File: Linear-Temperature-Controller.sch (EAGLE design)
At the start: 51 parts, among them IC1 LM393D, IC2 MEGA8-AI, IC3 AD5624R, IC4 AD5262, T1 MMBT3904, T2 MMBT3904

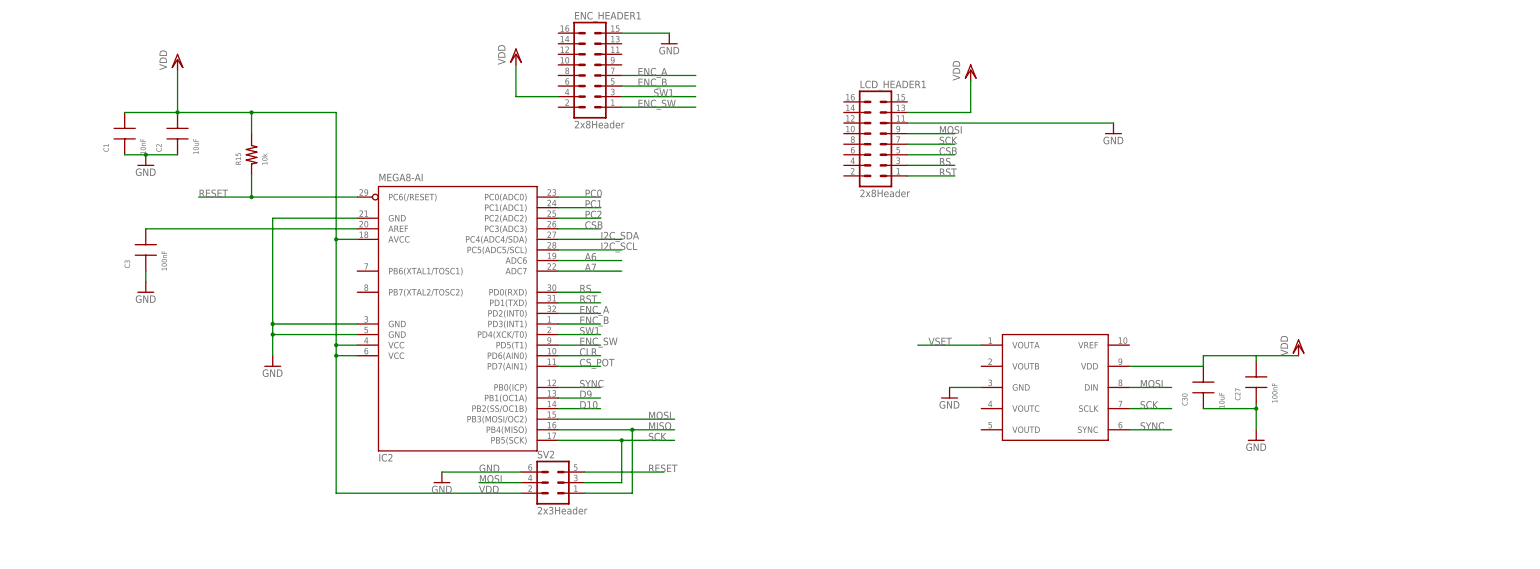
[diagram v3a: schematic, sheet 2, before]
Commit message: Replace microcontroller with Teensy
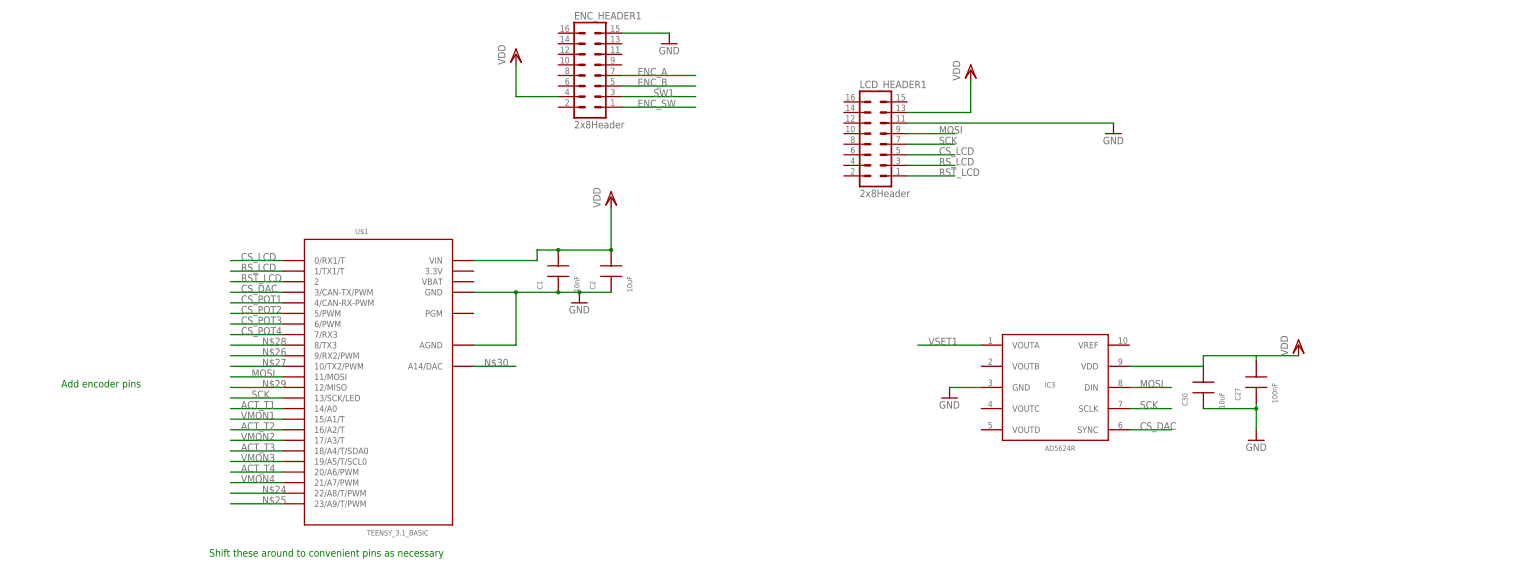
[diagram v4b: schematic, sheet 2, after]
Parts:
- removed C3: 100nF, rlc-jqi:CAP0603
- removed IC2: MEGA8-AI, atmel:MEGA8-AI
- removed R15: 10k, rlc-jqi:RES0603
- removed SV2: 2x3Header, con-lstb:MA03-2
- added CL2: 10nF, rcl:C-USC0805
- added CR2: 10uF, rcl:C-USC0805
- added IC5: OP27, opamp-jqi:OPAMP-SO
- added JP6: (no value), pinhead:PINHD-1X4
- added R18: 10k, rlc-jqi:RES0805
- added U$1: TEENSY_3.1_BASIC, mcu-accessories:TEENSY_3.1_BASIC
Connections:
- net VSET renamed VSET1
- removed net A6: IC2.ADC6
- removed net A7: IC2.ADC7
- removed net CLR: IC2.PD6(AIN0)
- removed net CSB: IC2.PC3(ADC3), LCD_HEADER1.5
- removed net CS_POT: IC2.PD7(AIN1), IC4.CS
- removed net D10: IC2.PB2(SS/OC1B)
- removed net D9: IC2.PB1(OC1A)
- removed net I2C_SCL: IC2.PC5(ADC5/SCL)
- removed net I2C_SDA: IC2.PC4(ADC4/SDA)
- removed net MISO: IC2.PB4(MISO), SV2.1
- removed net N$16: C3.P$2, IC2.AREF
- removed net PC0: IC2.PC0(ADC0)
- removed net PC1: IC2.PC1(ADC1)
- removed net PC2: IC2.PC2(ADC2)
- removed net RESET: IC2.PC6(/RESET), R15.P$1, SV2.5
- removed net RS: IC2.PD0(RXD), LCD_HEADER1.3
- removed net RST: IC2.PD1(TXD), LCD_HEADER1.1
- removed net SYNC: IC2.PB0(ICP), IC3.SYNC
- new net ACT_T1: R18.P$1, U$1.14/A0
- new net ACT_T2: U$1.16/A2/T
- new net ACT_T3: U$1.18/A4/T/SDA0
- new net ACT_T4: U$1.20/A6/PWM
- new net CS_DAC: IC3.SYNC, U$1.3/CAN-TX/PWM
- new net CS_LCD: LCD_HEADER1.5, U$1.0/RX1/T
- new net CS_POT1: IC4.CS, U$1.4/CAN-RX-PWM
- new net CS_POT2: U$1.5/PWM
- new net CS_POT3: U$1.6/PWM
- new net CS_POT4: U$1.7/RX3
- new net N$13: IC5.+IN, JP6.1, U1.9/S+
- new net N$21: JP6.3, U1.12/OUTB
- new net N$22: JP6.4, U1.11/OUTA
- new net N$23: IC5.-IN, IC5.OUT, R18.P$2, U1.8/SG
- new net N$24: U$1.22/A8/T/PWM
- new net N$25: U$1.23/A9/T/PWM
- new net N$26: U$1.9/RX2/PWM
- new net N$27: U$1.10/TX2/PWM
- new net N$28: U$1.8/TX3
- new net N$29: U$1.12/MISO
- new net N$30: U$1.A14/DAC
- new net RST_LCD: LCD_HEADER1.1, U$1.2
- new net RS_LCD: LCD_HEADER1.3, U$1.1/TX1/T
- new net VMON1: U$1.15/A1/T
- new net VMON2: U$1.17/A3/T
- new net VMON3: U$1.19/A5/T/SCL0
- new net VMON4: U$1.21/A7/PWM
- net ENC_A: no longer IC2.PD2(INT0)
- net ENC_B: no longer IC2.PD3(INT1)
- net ENC_SW: no longer IC2.PD5(T1)
- net GND: now also CL2.2, CR2.2, IC5.V-, JP6.2, U$1.AGND, U$1.GND; no longer C3.P$1, IC2.GND, IC2.GND@1, IC2.GND@2, SV2.6
- net MOSI: now also U$1.11/MOSI; no longer IC2.PB3(MOSI/OC2), SV2.4
- net N$19: now also U1.7/I
- net SCK: now also U$1.13/SCK/LED; no longer IC2.PB5(SCK), SV2.3
- net SW1: no longer IC2.PD4(XCK/T0)
- net VDD: now also CL2.1, CR2.1, IC5.V+, U$1.VIN; no longer IC2.AVCC, IC2.VCC@1, IC2.VCC@2, R15.P$2, SV2.2
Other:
- note added: "5V input"
- note added: "Add encoder pins"
- note added: "Sensor+ Sensor- OutB OutA"
- note added: "Shift these around to convenient pins as necessary"
- note added: "VSS Input"
- note removed: "LCD pins"
- note removed: "decouples internal reference"
- moved on the sheet: C1, C2, R5

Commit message: Add differential amplifier, separate AGND from DGND
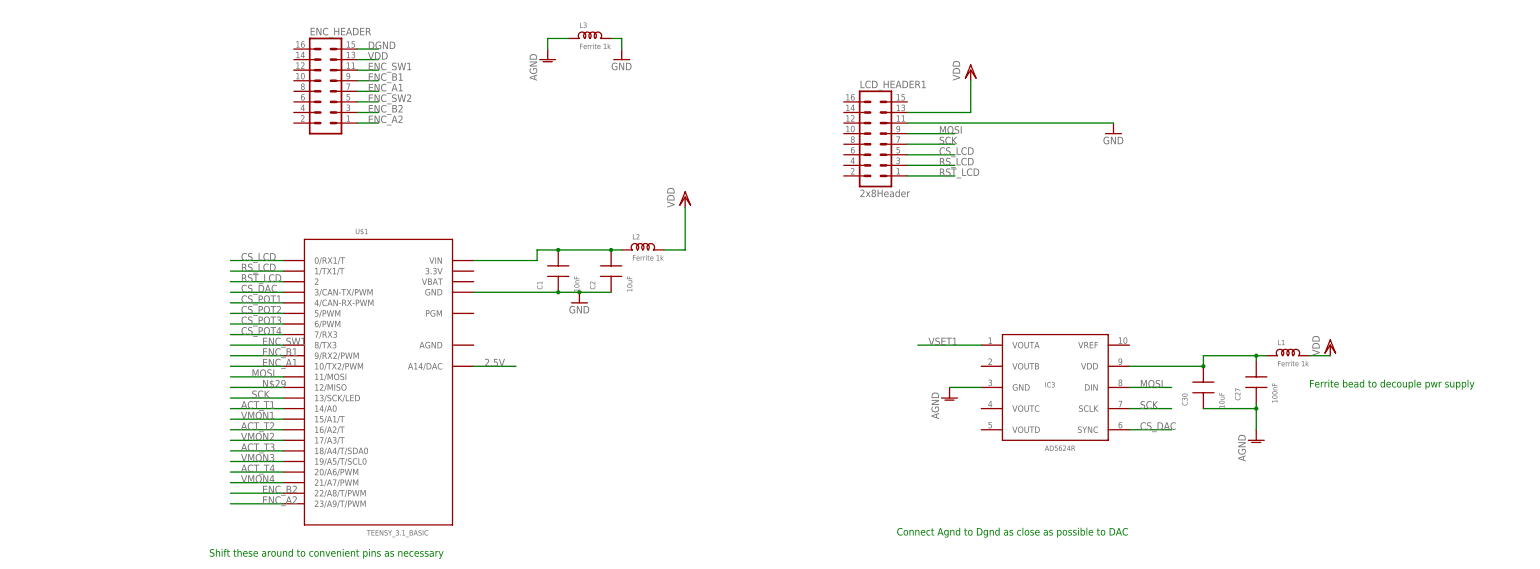
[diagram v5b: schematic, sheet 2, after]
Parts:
- removed ENC_HEADER1: 2x8Header, mcu-accessories:ML16
- added CL1: 10nF, rcl:C-USC0805
- added CR1: 10uF, rcl:C-USC0805
- added ENC_HEADER: (no value), aom_driver:ML16
- added IC2: (no value), Lin-Temp-Controller:INA159
- added L1, L2, L3: Ferrite 1k, rlc-jqi:INDUCTOR-0805
- added R15, R19: 100k 1%, rlc-jqi:RES0805
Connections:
- removed net ENC_A: ENC_HEADER1.7
- removed net ENC_B: ENC_HEADER1.5
- removed net ENC_SW: ENC_HEADER1.1
- removed net GND: C1.P$1, C2.P$1, C27.P$1, C30.P$1, C4.P$1, C5.P$1, CL2.2, CP1.-, CP2.2, CP3.-, CP4.-, CP5.-, CP6.2, CR2.2, ENC_HEADER1.15, IC1P.V-, IC3.GND, IC4.GND, IC4.VSS, IC5.V-, JP1.1, JP1.3, JP2.2, JP3.2, JP4.1, JP5.1, JP6.2, LCD_HEADER1.11, R1.P$1, R3.P$1, R6.2, R6.3, R7.3, T1.E, T2.E, U$1.AGND, U$1.GND, U1.13/GND
- removed net N$26: U$1.9/RX2/PWM
- removed net N$27: U$1.10/TX2/PWM
- removed net N$28: U$1.8/TX3
- removed net N$30: U$1.A14/DAC
- removed net SW1: ENC_HEADER1.3
- new net 2.5V: IC2.REF1, IC2.REF2, U$1.A14/DAC
- new net AGND: C27.P$1, C30.P$1, C4.P$1, C5.P$1, CL1.2, CL2.2, CP1.-, CP2.2, CP3.-, CP4.-, CP5.-, CP6.2, CR1.2, CR2.2, IC1P.V-, IC2.V-, IC3.GND, IC4.GND, IC4.VSS, IC5.V-, JP1.1, JP1.3, JP2.2, JP3.2, JP4.1, JP5.1, JP6.2, L3.P$1, R1.P$1, R3.P$1, R6.2, R6.3, R7.2, R7.3, T1.E, T2.E, U1.13/GND
- new net DGND: C1.P$1, C2.P$1, ENC_HEADER.15, L3.P$2, LCD_HEADER1.11, U$1.GND
- new net ENC_A1: ENC_HEADER.7, U$1.10/TX2/PWM
- new net ENC_A2: ENC_HEADER.1, U$1.23/A9/T/PWM
- new net ENC_B1: ENC_HEADER.9, U$1.9/RX2/PWM
- new net ENC_B2: ENC_HEADER.3, U$1.22/A8/T/PWM
- new net ENC_SW1: ENC_HEADER.11, U$1.8/TX3
- new net ENC_SW2: ENC_HEADER.5
- new net N$14: IC2.-IN, R15.P$1
- new net N$16: IC2.+IN, R19.P$1
- net N$21: now also R19.P$2
- net N$22: now also R15.P$2
- net N$24: now also C27.P$2, C30.P$2, IC3.VDD, L1.P$1; no longer U$1.22/A8/T/PWM
- net N$25: now also C1.P$2, C2.P$2, L2.P$1, U$1.VIN; no longer U$1.23/A9/T/PWM
- net VDD: now also CL1.1, CR1.1, ENC_HEADER.13, IC2.V+, L1.P$2, L2.P$2; no longer C1.P$2, C2.P$2, C27.P$2, C30.P$2, ENC_HEADER1.4, IC3.VDD, U$1.VIN
- net VMON1: now also IC2.OUT, IC2.SENSE
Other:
- note added: "Ask Allessandro about how/if to decouple analog/digital supplies/gnd"
- note added: "Connect Agnd to Dgnd as close as possible to DAC"
- note added: "Ferrite bead to decouple pwr supply"
- note added: "Sensor+ Sensor- OutB (TEC+) OutA (TEC-)"
- note added: "ferrite + caps"
- note removed: "Add encoder pins"
- note removed: "Sensor+ Sensor- OutB OutA"

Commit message: Schematic progress
Add 2.5V ref, swap trimpot package, add monitor headers
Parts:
- added C3: 1000pF, rlc-jqi:CAP0805
- added C6: .1uF, rlc-jqi:CAP0805
- added IC6: (no value), Lin-Temp-Controller:TS6001
- added JP7, JP8, JP9: (no value), pinhead:PINHD-1X2
- R6, R7: device jqi_passives:R_TRIMPOT_SMD_BOURNS-3224XBOURNS -> Lin-Temp-Controller:64XR
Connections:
- new net MON: JP9.2, U$1.A14/DAC
- net 2.5V: now also C3.P$2, IC6.OUT; no longer U$1.A14/DAC
- net ACT_T1: now also JP7.2
- net AGND: now also C3.P$1, C6.P$1, IC6.GND, JP7.1, JP8.1, JP9.1
- net VDD: now also C6.P$2, IC6.IN
- net VMON1: now also JP8.2
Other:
- note added: "twisted pair to front panel"
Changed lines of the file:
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@@
 <part name="T2" library="Lin-Temp-Controller" deviceset="MMBT3904" device=""/>
 <part name="IC1" library="Lin-Temp-Controller" deviceset="LM393" device="D"/>
-<part name="R6" library="jqi_passives" deviceset="R_TRIMPOT_SMD_BOURNS-3224X" device="BOURNS" value="10k"/>
-<part name="R7" library="jqi_passives" deviceset="R_TRIMPOT_SMD_BOURNS-3224X" device="BOURNS" value="10k"/>
+<part name="R6" library="Lin-Temp-Controller" deviceset="64XR" device="" value="10k"/>
+<part name="R7" library="Lin-Temp-Controller" deviceset="64XR" device="" value="10k"/>
 <part name="VDD3" library="supply1" deviceset="VDD" device=""/>
 <part name="VDD4" library="supply1" deviceset="VDD" device=""/>
@@
 <part name="AGND14" library="supply1" deviceset="AGND" device=""/>
 <part name="AGND15" library="supply1" deviceset="AGND" device=""/>
+<part name="IC6" library="Lin-Temp-Controller" deviceset="TS6001" device=""/>
+<part name="C3" library="rlc-jqi" deviceset="CAP" device="0805" value="1000pF"/>
+<part name="C6" library="rlc-jqi" deviceset="CAP" device="0805" value=".1uF"/>
+<part name="VDD13" library="supply1" deviceset="VDD" device=""/>
+<part name="AGND16" library="supply1" deviceset="AGND" device=""/>
+<part name="JP7" library="pinhead" deviceset="PINHD-1X2" device=""/>
+<part name="AGND17" library="supply1" deviceset="AGND" device=""/>
+<part name="JP8" library="pinhead" deviceset="PINHD-1X2" device=""/>
+<part name="AGND18" library="supply1" deviceset="AGND" device=""/>
+<part name="JP9" library="pinhead" deviceset="PINHD-1X2" device=""/>
+<part name="AGND19" library="supply1" deviceset="AGND" device=""/>
 </parts>
 <sheets>
@@
 <text x="27.94" y="60.96" size="1.778" layer="91">ferrite + caps</text>
 <text x="-30.48" y="-96.52" size="1.778" layer="91">Ask Allessandro about how/if to decouple analog/digital supplies/gnd</text>
+<text x="195.58" y="-96.52" size="1.778" layer="91">twisted pair to front panel</text>
 </plain>
 <instances>
@@
 <instance part="IC1" gate="B" x="-116.84" y="-17.78"/>
 <instance part="IC1" gate="P" x="-162.56" y="40.64"/>
-<instance part="R6" gate="G$1" x="-144.78" y="33.02" rot="R270"/>
-<instance part="R7" gate="G$1" x="-144.78" y="-25.4" rot="R270"/>
+<instance part="R6" gate="G$1" x="-144.78" y="33.02" rot="R180"/>
+<instance part="R7" gate="G$1" x="-144.78" y="-27.94" rot="R180"/>
 <instance part="VDD3" gate="G$1" x="-162.56" y="58.42"/>
 <instance part="VDD4" gate="G$1" x="-144.78" y="0"/>
@@
 <instance part="AGND11" gate="VR1" x="187.96" y="15.24"/>
 <instance part="AGND12" gate="VR1" x="251.46" y="40.64"/>
+<instance part="IC6" gate="G$1" x="205.74" y="-20.32"/>
+<instance part="C3" gate="G$1" x="205.74" y="-35.56" rot="R180"/>
+<instance part="C6" gate="G$1" x="220.98" y="-5.08" rot="R90"/>
+<instance part="VDD13" gate="G$1" x="193.294" y="2.54"/>
+<instance part="AGND16" gate="VR1" x="220.98" y="-25.4"/>
+<instance part="JP7" gate="G$1" x="172.72" y="-81.28" rot="R180"/>
+<instance part="AGND17" gate="VR1" x="190.5" y="-86.36"/>
+<instance part="JP8" gate="G$1" x="200.66" y="-81.28" rot="R180"/>
+<instance part="AGND18" gate="VR1" x="218.44" y="-86.36"/>
+<instance part="JP9" gate="G$1" x="228.6" y="-81.28" rot="R180"/>
+<instance part="AGND19" gate="VR1" x="246.38" y="-86.36"/>
 </instances>
 <busses>
@@
 <segment>
 <pinref part="R6" gate="G$1" pin="3"/>
+<pinref part="AGND2" gate="VR1" pin="AGND"/>
 <wire x1="-144.78" y1="25.4" x2="-144.78" y2="22.86" width="0.1524" layer="91"/>
 <pinref part="R6" gate="G$1" pin="2"/>
-<wire x1="-139.7" y1="30.48" x2="-139.7" y2="25.4" width="0.1524" layer="91"/>
-<wire x1="-139.7" y1="25.4" x2="-144.78" y2="25.4" width="0.1524" layer="91"/>
-<pinref part="AGND2" gate="VR1" pin="AGND"/>
+<wire x1="-149.86" y1="33.02" x2="-152.4" y2="33.02" width="0.1524" layer="91"/>
+<wire x1="-152.4" y1="33.02" x2="-152.4" y2="22.86" width="0.1524" layer="91"/>
+<wire x1="-152.4" y1="22.86" x2="-144.78" y2="22.86" width="0.1524" layer="91"/>
 </segment>
 <segment>
@@
 <pinref part="R7" gate="G$1" pin="3"/>
 <pinref part="AGND4" gate="VR1" pin="AGND"/>
-<wire x1="-144.78" y1="-35.56" x2="-144.78" y2="-33.02" width="0.1524" layer="91"/>
 <pinref part="R7" gate="G$1" pin="2"/>
-<wire x1="-139.7" y1="-27.94" x2="-139.7" y2="-35.56" width="0.1524" layer="91"/>
-<wire x1="-139.7" y1="-35.56" x2="-144.78" y2="-35.56" width="0.1524" layer="91"/>
+<wire x1="-149.86" y1="-27.94" x2="-149.86" y2="-35.56" width="0.1524" layer="91"/>
+<wire x1="-149.86" y1="-35.56" x2="-144.78" y2="-35.56" width="0.1524" layer="91"/>
 </segment>
 <segment>
@@
 <pinref part="AGND3" gate="VR1" pin="AGND"/>
 <wire x1="-162.56" y1="30.48" x2="-162.56" y2="33.02" width="0.1524" layer="91"/>
+</segment>
+<segment>
+<pinref part="IC6" gate="G$1" pin="GND"/>
+<pinref part="AGND16" gate="VR1" pin="AGND"/>
+<wire x1="215.9" y1="-20.32" x2="220.98" y2="-20.32" width="0.1524" layer="91"/>
+<wire x1="220.98" y1="-20.32" x2="220.98" y2="-22.86" width="0.1524" layer="91"/>
+<pinref part="C6" gate="G$1" pin="P$1"/>
+<wire x1="220.98" y1="-10.16" x2="220.98" y2="-20.32" width="0.1524" layer="91"/>
+<wire x1="215.9" y1="-20.32" x2="215.9" y2="-35.56" width="0.1524" layer="91"/>
+<pinref part="C3" gate="G$1" pin="P$1"/>
+<wire x1="215.9" y1="-35.56" x2="210.82" y2="-35.56" width="0.1524" layer="91"/>
+<junction x="215.9" y="-20.32"/>
+</segment>
+<segment>
+<pinref part="JP7" gate="G$1" pin="1"/>
+<wire x1="175.26" y1="-83.82" x2="190.5" y2="-83.82" width="0.1524" layer="91"/>
+<pinref part="AGND17" gate="VR1" pin="AGND"/>
+</segment>
+<segment>
+<pinref part="JP8" gate="G$1" pin="1"/>
+<wire x1="203.2" y1="-83.82" x2="218.44" y2="-83.82" width="0.1524" layer="91"/>
+<pinref part="AGND18" gate="VR1" pin="AGND"/>
+</segment>
+<segment>
+<pinref part="JP9" gate="G$1" pin="1"/>
+<wire x1="231.14" y1="-83.82" x2="246.38" y2="-83.82" width="0.1524" layer="91"/>
+<pinref part="AGND19" gate="VR1" pin="AGND"/>
 </segment>
 </net>
@@
 <wire x1="220.98" y1="30.48" x2="233.68" y2="30.48" width="0.1524" layer="91"/>
 </segment>
+<segment>
+<pinref part="C6" gate="G$1" pin="P$2"/>
+<wire x1="193.294" y1="0" x2="193.04" y2="0" width="0.1524" layer="91"/>
+<wire x1="220.98" y1="0" x2="193.294" y2="0" width="0.1524" layer="91"/>
+<wire x1="193.04" y1="0" x2="193.04" y2="-15.24" width="0.1524" layer="91"/>
+<pinref part="IC6" gate="G$1" pin="IN"/>
+<wire x1="193.04" y1="-15.24" x2="195.58" y2="-15.24" width="0.1524" layer="91"/>
+<pinref part="VDD13" gate="G$1" pin="VDD"/>
+<junction x="193.04" y="0"/>
+</segment>
 </net>
 <net name="VSS" class="0">
@@
 <wire x1="-144.78" y1="45.72" x2="-144.78" y2="43.18" width="0.1524" layer="91"/>
 <pinref part="IC1" gate="A" pin="+IN"/>
-<wire x1="-144.78" y1="43.18" x2="-144.78" y2="38.1" width="0.1524" layer="91"/>
+<wire x1="-144.78" y1="43.18" x2="-144.78" y2="40.64" width="0.1524" layer="91"/>
 <wire x1="-127" y1="43.18" x2="-134.62" y2="43.18" width="0.1524" layer="91"/>
 <pinref part="TP1" gate="G$1" pin="P$1"/>
@@
 <label x="132.08" y="-20.32" size="1.778" layer="95"/>
 </segment>
+<segment>
+<pinref part="JP7" gate="G$1" pin="2"/>
+<wire x1="175.26" y1="-81.28" x2="190.5" y2="-81.28" width="0.1524" layer="91"/>
+<label x="180.34" y="-81.28" size="1.778" layer="95"/>
+</segment>
 </net>
 <net name="VSET1" class="0">
@@
 <label x="228.6" y="25.4" size="1.778" layer="95"/>
 <junction x="226.06" y="25.4"/>
+</segment>
+<segment>
+<pinref part="JP8" gate="G$1" pin="2"/>
+<wire x1="203.2" y1="-81.28" x2="218.44" y2="-81.28" width="0.1524" layer="91"/>
+<label x="208.28" y="-81.28" size="1.778" layer="95"/>
 </segment>
 </net>
@@
 <label x="177.8" y="45.72" size="1.778" layer="95"/>
 <junction x="187.96" y="45.72"/>
+</segment>
+<segment>
+<pinref part="C3" gate="G$1" pin="P$2"/>
+<wire x1="200.66" y1="-35.56" x2="193.04" y2="-35.56" width="0.1524" layer="91"/>
+<wire x1="193.04" y1="-35.56" x2="193.04" y2="-25.4" width="0.1524" layer="91"/>
+<pinref part="IC6" gate="G$1" pin="OUT"/>
+<wire x1="193.04" y1="-25.4" x2="195.58" y2="-25.4" width="0.1524" layer="91"/>
+<wire x1="193.04" y1="-25.4" x2="182.88" y2="-25.4" width="0.1524" layer="91"/>
+<label x="185.42" y="-25.4" size="1.778" layer="95"/>
+</segment>
+</net>
+<net name="MON" class="0">
+<segment>
+<pinref part="JP9" gate="G$1" pin="2"/>
+<wire x1="231.14" y1="-81.28" x2="246.38" y2="-81.28" width="0.1524" layer="91"/>
+<label x="236.22" y="-81.28" size="1.778" layer="95"/>
 </segment>
 </net>
@@
 </segment>
 </net>
-<net name="2.5V" class="0">
-<segment>
-<pinref part="U$1" gate="G$1" pin="A14/DAC"/>
-<wire x1="109.22" y1="-2.54" x2="119.38" y2="-2.54" width="0.1524" layer="91"/>
-<label x="111.76" y="-2.54" size="1.778" layer="95"/>
-</segment>
-</net>
 <net name="ENC_SW2" class="0">
 <segment>
@@
 </segment>
 </net>
+<net name="MON" class="0">
+<segment>
+<pinref part="U$1" gate="G$1" pin="A14/DAC"/>
+<wire x1="109.22" y1="-2.54" x2="119.38" y2="-2.54" width="0.1524" layer="91"/>
+<label x="111.76" y="-2.54" size="1.778" layer="95"/>
+</segment>
+</net>
